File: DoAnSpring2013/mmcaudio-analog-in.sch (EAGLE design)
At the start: 24 parts, among them IC1 TL082, IC2 TL082

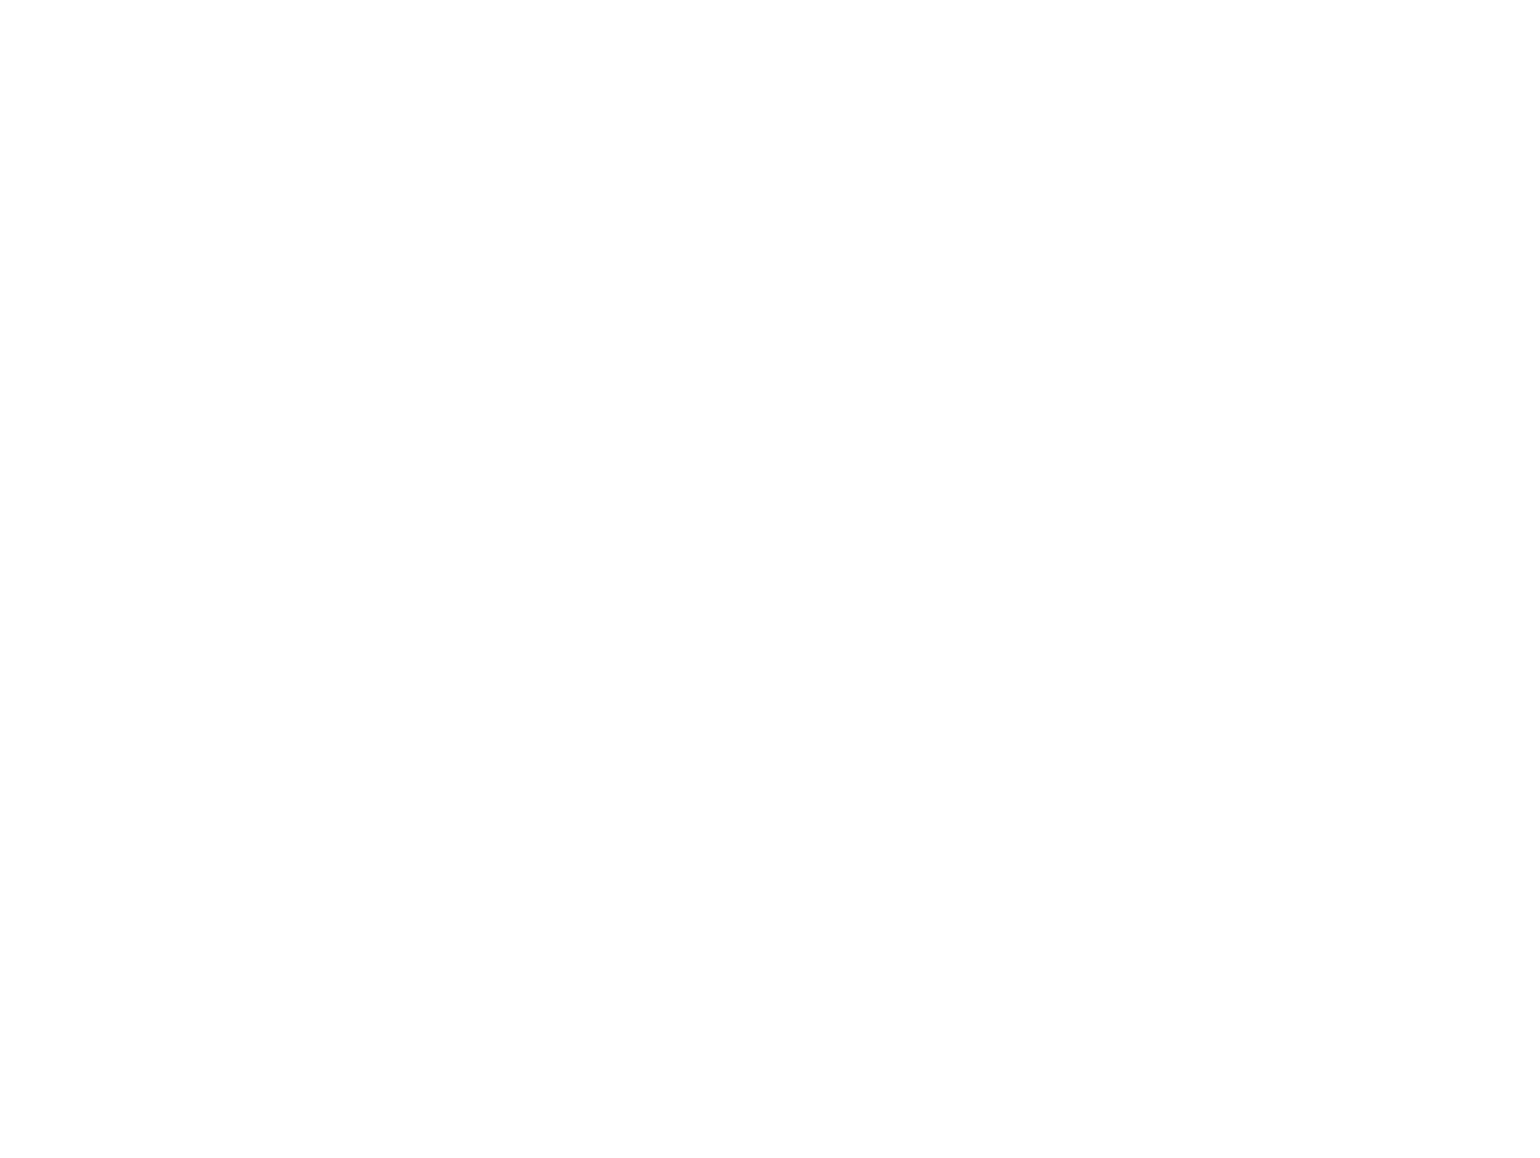
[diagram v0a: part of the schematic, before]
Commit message: begin routing main board
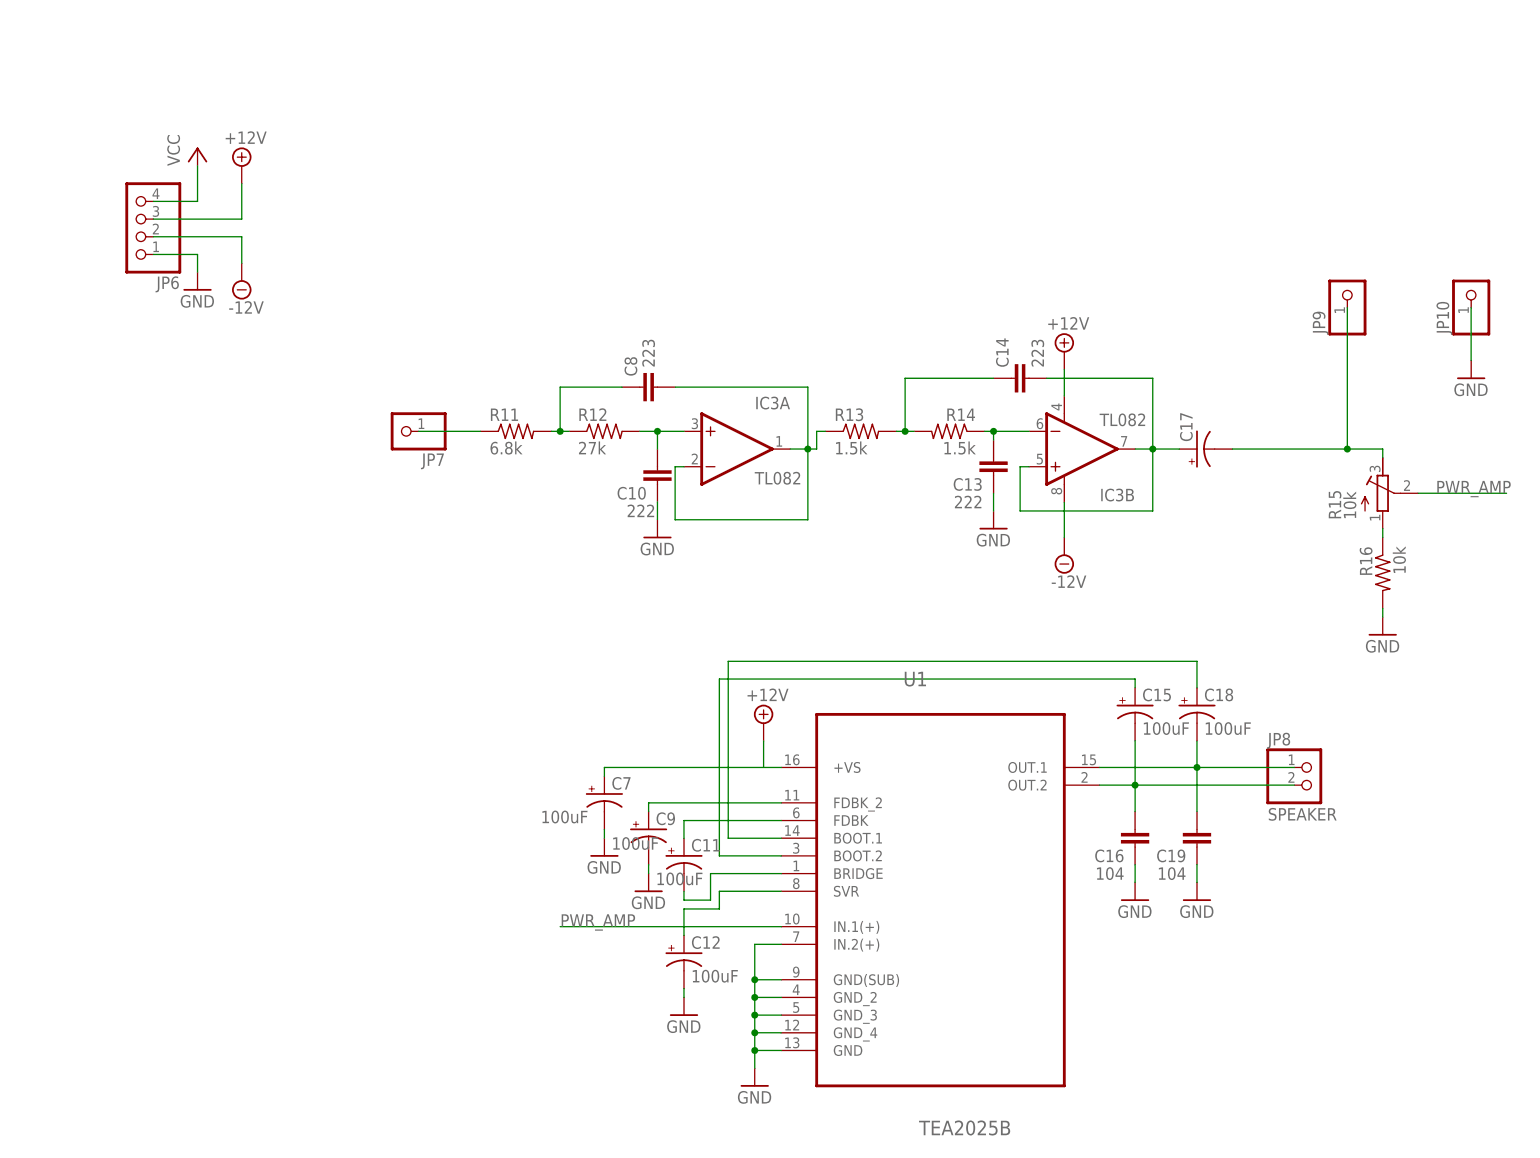
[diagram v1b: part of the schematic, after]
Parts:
- added C10, C13: 222, datle-discrete:C-EUCERAMIC-CAP-COMMON
- added C11, C12, C15, C18, C7, C9: 100uF, datle-discrete:CPOL-USSANYO_D
- added C14, C8: 223, datle-discrete:C-EUCERAMIC-CAP-COMMON
- added C16, C19: 104, datle-discrete:C-EUCERAMIC-CAP-COMMON
- added C17: (no value), datle-discrete:CPOL-USSANYO_D
- added IC3: TL082, datle-analogic:TL082
- added JP10, JP7, JP9: (no value), datle-conn:PINHD-1X1
- added JP6: (no value), pinhead:PINHD-1X4
- added JP8: SPEAKER, datle-conn:PINHD-1X20.5"
- added R11: 6.8k, datle-discrete:R-US_0207/10
- added R12: 27k, datle-discrete:R-US_0207/10
- added R13, R14: 1.5k, datle-discrete:R-US_0207/10
- added R15: 10k, datle-discrete:R-TRIMM64W
- added R16: 10k, datle-discrete:R-US_0207/10
- added U1: TEA2025B, datle-analogic:TEA2025B
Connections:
- new net N$14: C8.1, R11.2, R12.1
- new net N$15: C10.2, IC3A.+IN, R12.2
- new net N$16: C8.2, IC3A.-IN, IC3A.OUT, R13.1
- new net N$17: C14.1, R13.2, R14.2
- new net N$18: C13.2, IC3B.-IN, R14.1
- new net N$19: C14.2, C17.+, IC3B.+IN, IC3B.OUT
- new net N$20: JP7.1, R11.1
- new net N$21: C17.-, JP9.1, R15.E
- new net N$22: C9.+, U1.FDBK_2
- new net N$23: C11.+, U1.FDBK
- new net N$24: C11.-, U1.BRIDGE
- new net N$25: C18.-, C19.2, JP8.1, U1.OUT.1
- new net N$26: C18.+, U1.BOOT.1
- new net N$27: C15.-, C16.2, JP8.2, U1.OUT.2
- new net N$28: C15.+, U1.BOOT.2
- new net N$29: C12.+, U1.SVR
- new net N$30: R15.A, R16.1
- new net PWR_AMP: R15.S, U1.IN.1(+)
- net +12V: now also C7.+, IC3B.V-, JP6.3, U1.+VS
- net -12V: now also IC3B.V+, JP6.2
- net GND: now also C10.1, C12.-, C13.1, C16.1, C19.1, C7.-, C9.-, JP10.1, JP6.1, R16.2, U1.GND, U1.GND(SUB), U1.GND_2, U1.GND_3, U1.GND_4, U1.IN.2(+)
- net VCC: now also JP6.4
